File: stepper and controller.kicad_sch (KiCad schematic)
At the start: 30 parts

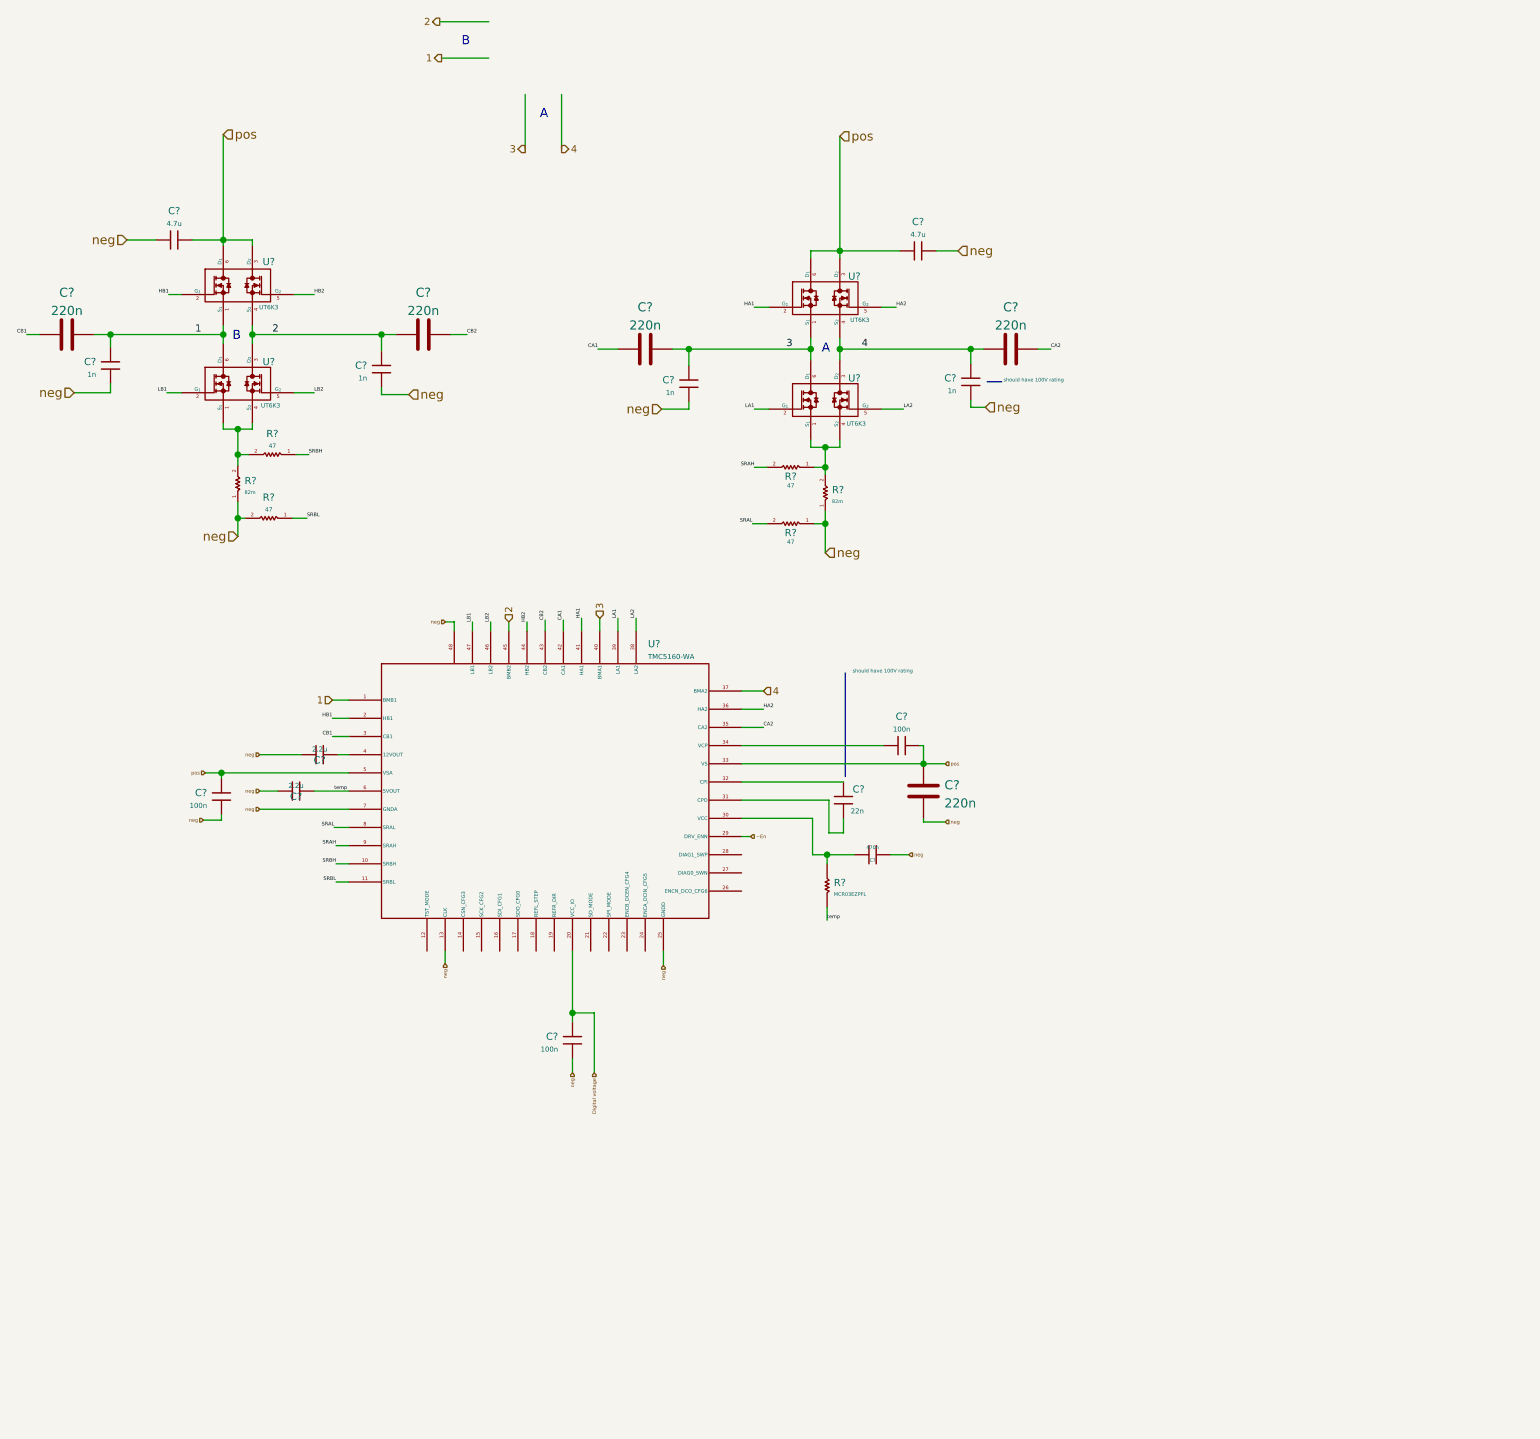
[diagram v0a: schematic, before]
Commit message: reference designator added
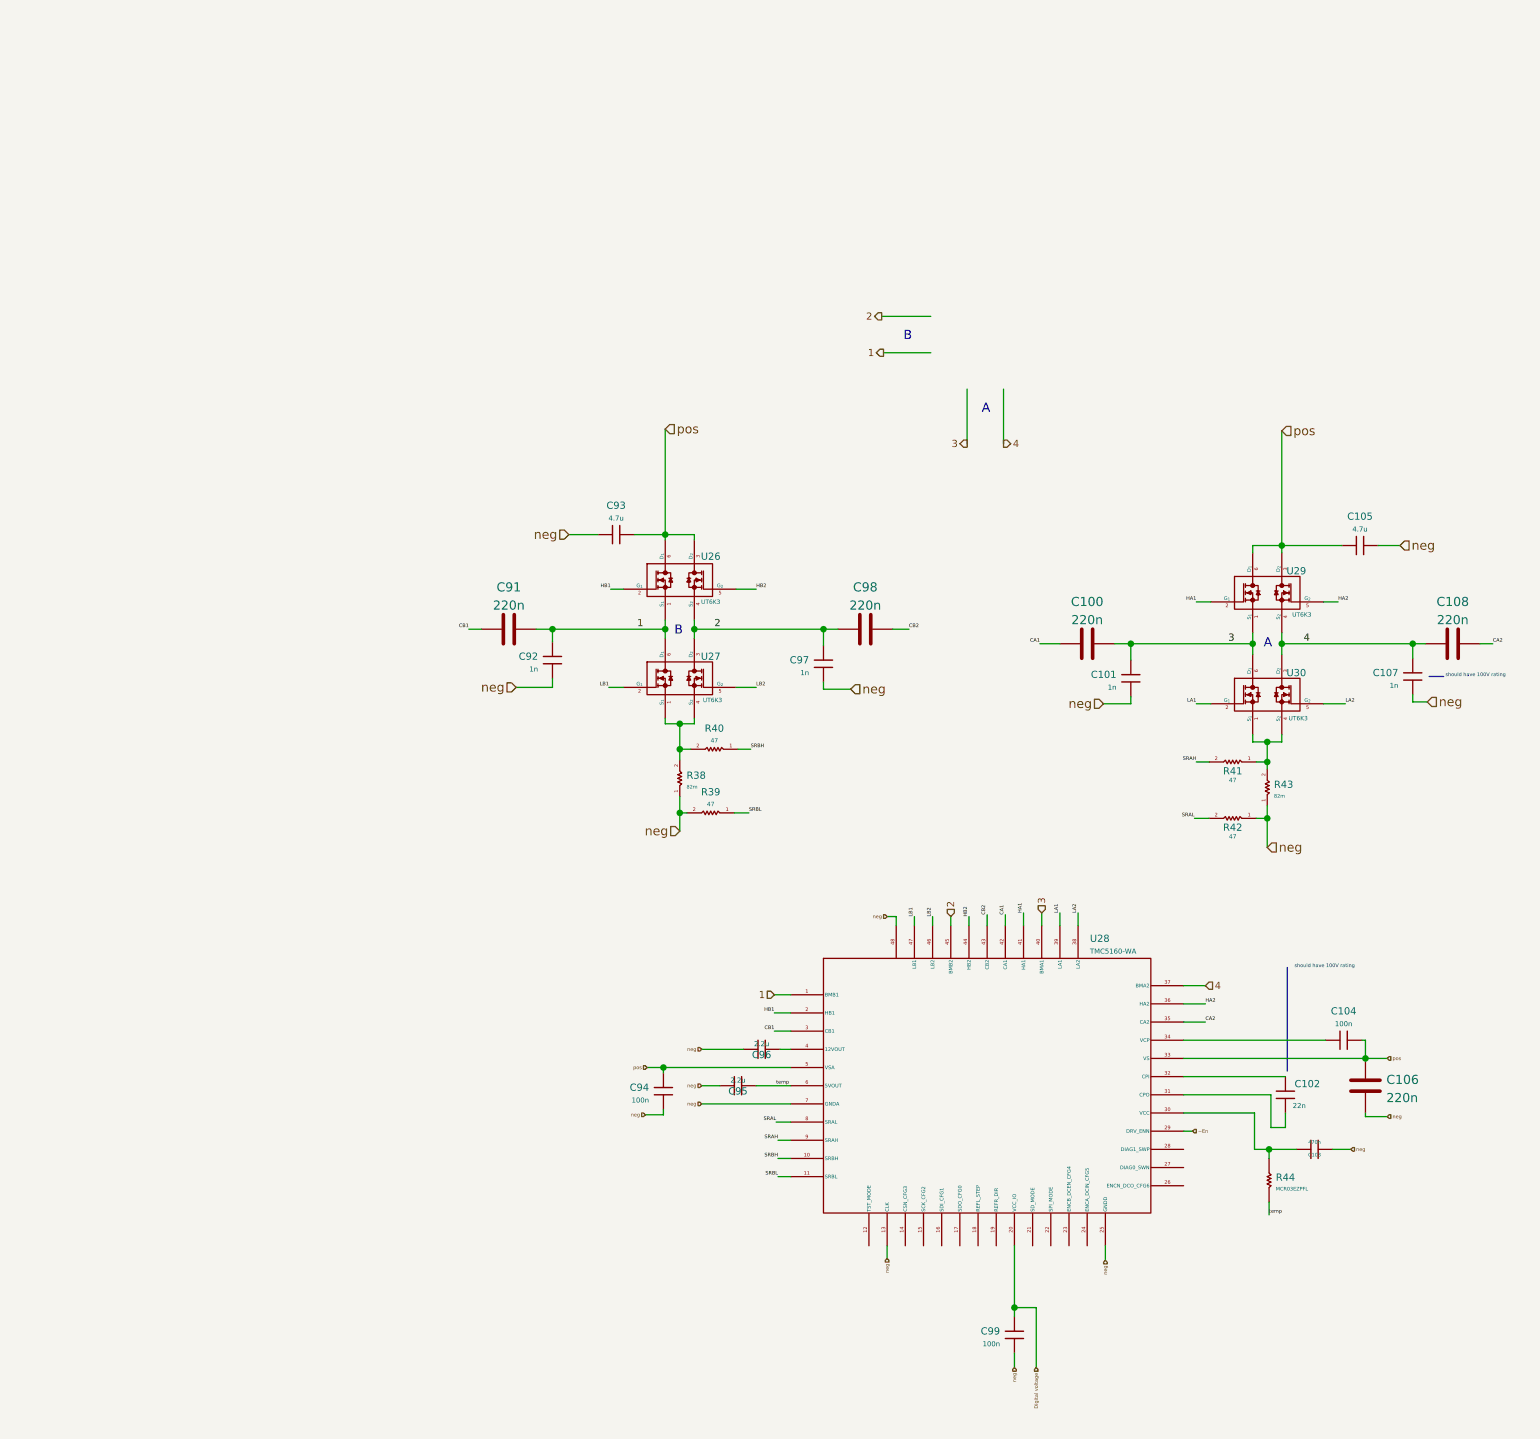
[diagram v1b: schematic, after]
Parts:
- gave numbers to parts that had none: 30
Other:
- moved on the sheet: C100, C101, C102, C103, C104, C105, C106, C107, C108, C91, C92, C93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

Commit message: updating schematics
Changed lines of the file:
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@@
   (symbol (lib_id "Capacitors:C0603X105J4RACTU") (at 175.768 161.544 0) (unit 1)
     (in_bom yes) (on_board yes)
-    (property "Reference" "C96" (id 0) (at 175.768 162.306 0)
-      (effects (font (size 1 1)))
+    (property "Reference" "C96" (id 0) (at 173.736 162.56 0)
+      (effects (font (size 0.5 0.5)))
     )
-    (property "Value" "2.2u" (id 1) (at 175.768 160.782 0)
+    (property "Value" "2.2u" (id 1) (at 173.736 160.528 0)
       (effects (font (size 0.7 0.7)))
     )
@@
   (symbol (lib_id "Capacitors:C0603X105J4RACTU") (at 172.466 166.624 0) (unit 1)
     (in_bom yes) (on_board yes)
-    (property "Reference" "C95" (id 0) (at 172.466 167.386 0)
-      (effects (font (size 1 1)))
+    (property "Reference" "C95" (id 0) (at 170.688 167.64 0)
+      (effects (font (size 0.5 0.5)))
     )
-    (property "Value" "2.2u" (id 1) (at 172.466 165.862 0)
+    (property "Value" "2.2u" (id 1) (at 170.688 165.608 0)
       (effects (font (size 0.7 0.7)))
     )

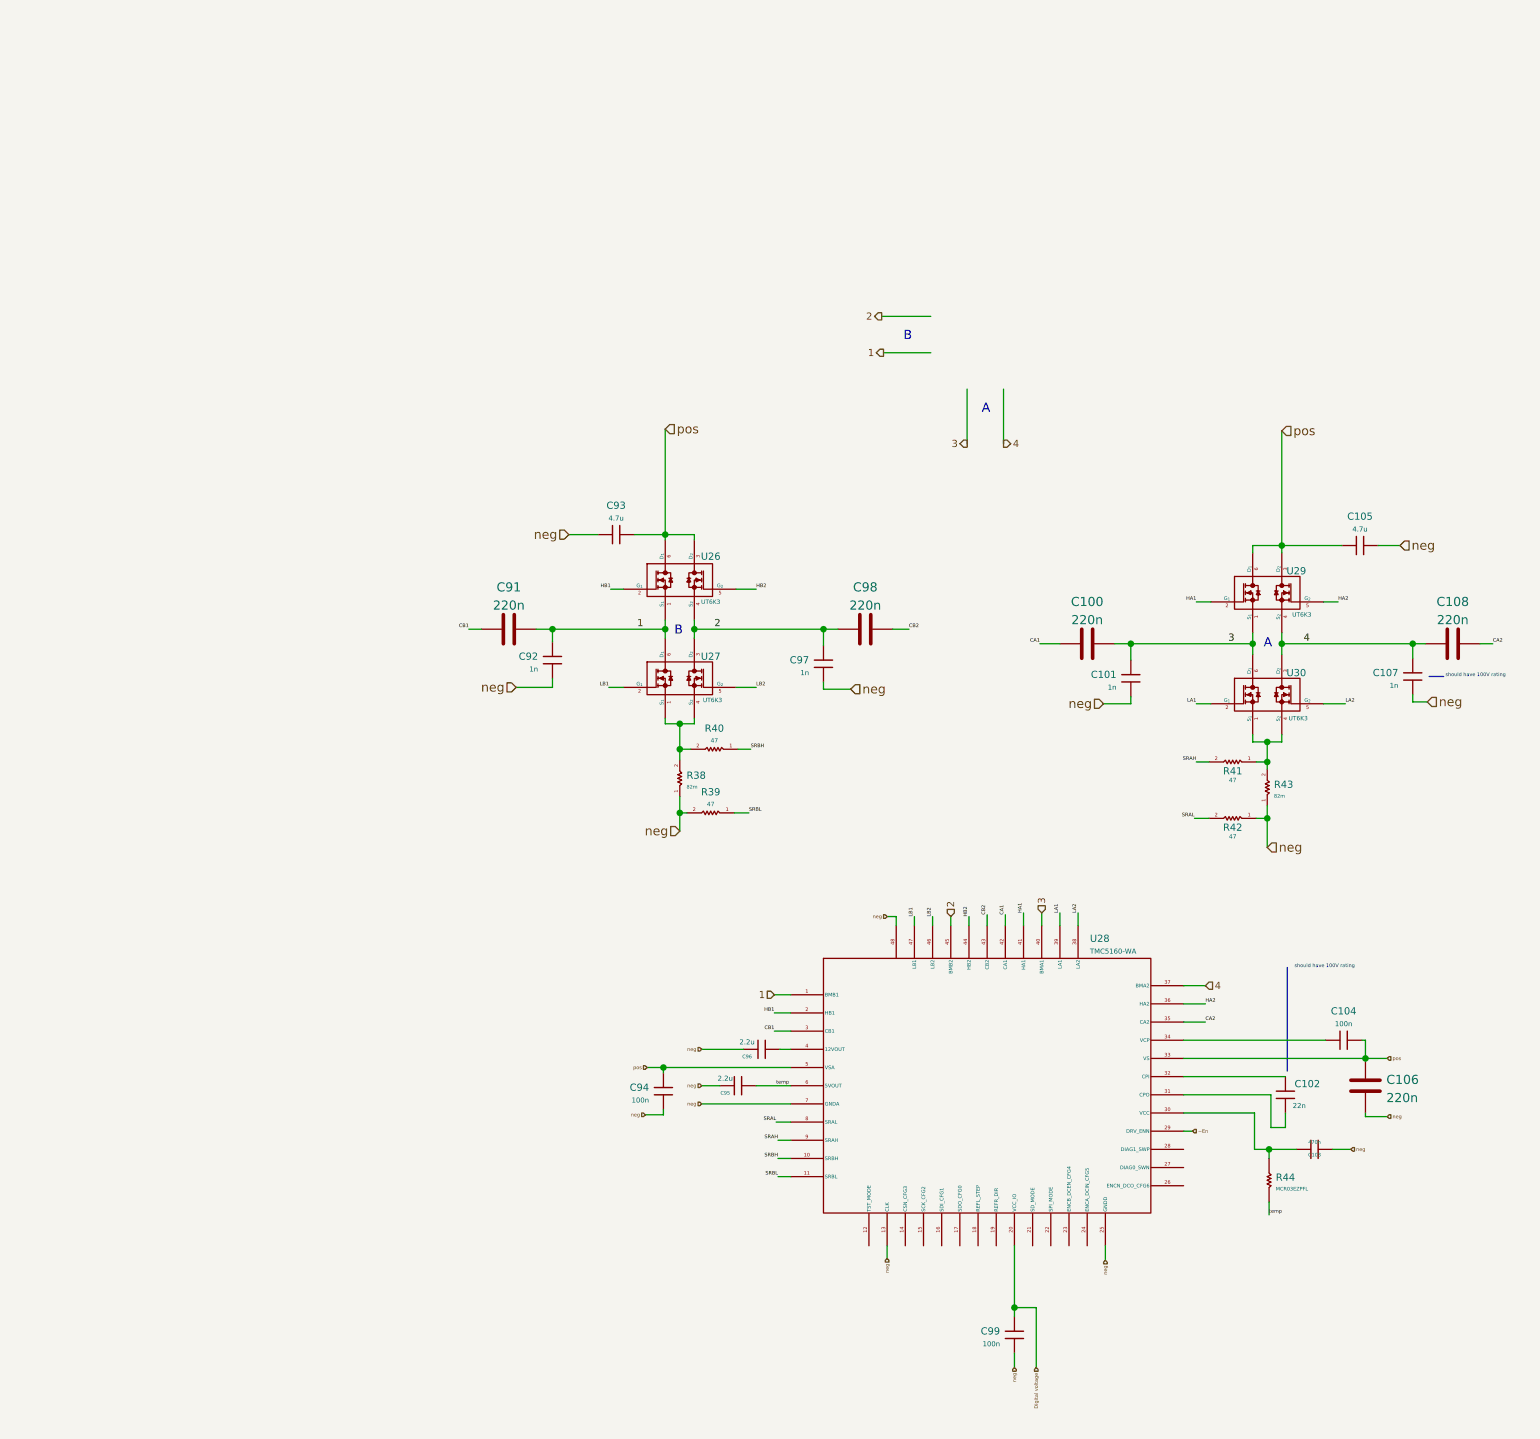
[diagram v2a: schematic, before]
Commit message: changing some capacitors
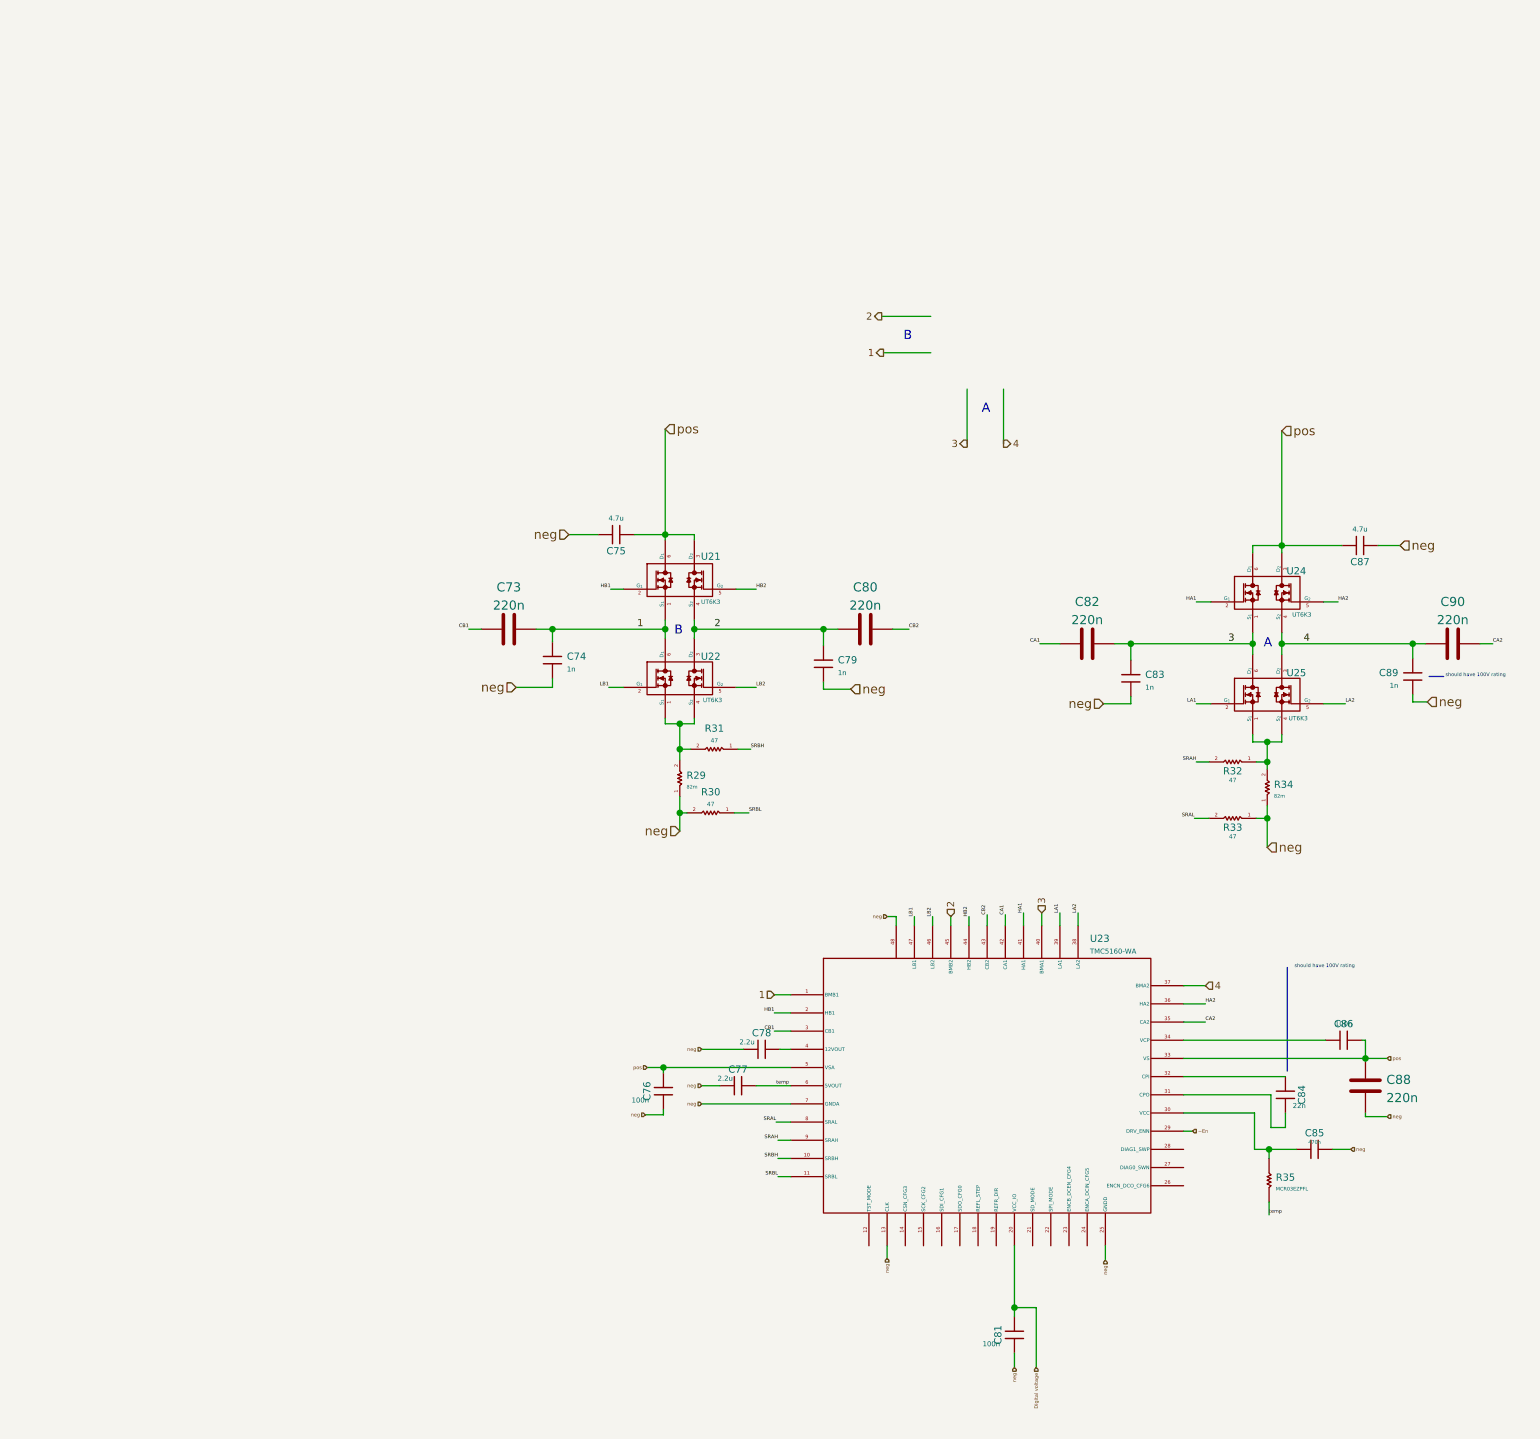
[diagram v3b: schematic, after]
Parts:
- C74: renamed from C92; symbol Capacitors:C0603X105J4RACTU -> Capacitors:C0603xxxxxxxxxxx
- C75: renamed from C93; symbol Capacitors:C0603X105J4RACTU -> Capacitors:C0603xxxxxxxxxxx
- C76: renamed from C94; symbol Capacitors:C0603X105J4RACTU -> Capacitors:C0603xxxxxxxxxxx
- C77: renamed from C95; symbol Capacitors:C0603X105J4RACTU -> Capacitors:C0603xxxxxxxxxxx
- C78: renamed from C96; symbol Capacitors:C0603X105J4RACTU -> Capacitors:C0603xxxxxxxxxxx
- C79: renamed from C97; symbol Capacitors:C0603X105J4RACTU -> Capacitors:C0603xxxxxxxxxxx
- C81: renamed from C99; symbol Capacitors:C0603X105J4RACTU -> Capacitors:C0603xxxxxxxxxxx
- C83: renamed from C101; symbol Capacitors:C0603X105J4RACTU -> Capacitors:C0603xxxxxxxxxxx
- C84: renamed from C102; symbol Capacitors:C0603X105J4RACTU -> Capacitors:C0603xxxxxxxxxxx
- C85: renamed from C103; symbol Capacitors:C0603X105J4RACTU -> Capacitors:C0603xxxxxxxxxxx
- C86: renamed from C104; symbol Capacitors:C0603X105J4RACTU -> Capacitors:C0603xxxxxxxxxxx
- C87: renamed from C105; symbol Capacitors:C0603X105J4RACTU -> Capacitors:C0603xxxxxxxxxxx
- C89: renamed from C107; symbol Capacitors:C0603X105J4RACTU -> Capacitors:C0603xxxxxxxxxxx
- renumbered C91 to C73, C98 to C80, C100 to C82, C106 to C88, C108 to C90, R38 to R29, R39 to R30, R40 to R31, R41 to R32, R42 to R33, R43 to R34, R44 to R35, U26 to U21, U27 to U22, U28 to U23, U29 to U24, U30 to U25
